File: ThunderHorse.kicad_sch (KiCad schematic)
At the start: 0 parts

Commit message: Schematic structure
Added new schematic sheets.
Updated the main project.
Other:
- added sheet ESC (ESC.kicad_sch)
- added sheet MCU (MCU.kicad_sch)
- added sheet Power (Power.kicad_sch)
- added sheet Sensors (Sensors.kicad_sch)
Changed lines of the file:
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@@
 		(company "Chapuzas S.L.")
+	)
+	(sheet
+		(at 52.07 92.71)
+		(size 88.9 58.42)
+		(exclude_from_sim no)
+		(in_bom yes)
+		(on_board yes)
+		(dnp no)
+		(fields_autoplaced yes)
+		(stroke
+			(width 0.1524)
+			(type solid)
+		)
+		(fill
+			(color 0 0 0 0.0000)
+		)
+		(property "Sheetname" "MCU"
+			(at 52.07 91.9984 0)
+			(effects
+				(font
+					(size 1.27 1.27)
+				)
+				(justify left bottom)
+			)
+		)
+		(property "Sheetfile" "MCU.kicad_sch"
+			(at 52.07 151.7146 0)
+			(effects
+				(font
+					(size 1.27 1.27)
+				)
+				(justify left top)
+			)
+		)
+		(instances
+			(project "ThunderHorse"
+				(path "/ac187c6c-fa53-41cc-bce1-6f39a42a92e8"
+					(page "3")
+				)
+			)
+		)
+	)
+	(sheet
+		(at 154.94 92.71)
+		(size 88.9 58.42)
+		(exclude_from_sim no)
+		(in_bom yes)
+		(on_board yes)
+		(dnp no)
+		(fields_autoplaced yes)
+		(stroke
+			(width 0.1524)
+			(type solid)
+		)
+		(fill
+			(color 0 0 0 0.0000)
+		)
+		(property "Sheetname" "Sensors"
+			(at 154.94 91.9984 0)
+			(effects
+				(font
+					(size 1.27 1.27)
+				)
+				(justify left bottom)
+			)
+		)
+		(property "Sheetfile" "Sensors.kicad_sch"
+			(at 154.94 151.7146 0)
+			(effects
+				(font
+					(size 1.27 1.27)
+				)
+				(justify left top)
+			)
+		)
+		(instances
+			(project "ThunderHorse"
+				(path "/ac187c6c-fa53-41cc-bce1-6f39a42a92e8"
+					(page "5")
+				)
+			)
+		)
+	)
+	(sheet
+		(at 154.94 26.67)
+		(size 88.9 58.42)
+		(exclude_from_sim no)
+		(in_bom yes)
+		(on_board yes)
+		(dnp no)
+		(fields_autoplaced yes)
+		(stroke
+			(width 0.1524)
+			(type solid)
+		)
+		(fill
+			(color 0 0 0 0.0000)
+		)
+		(property "Sheetname" "ESC"
+			(at 154.94 25.9584 0)
+			(effects
+				(font
+					(size 1.27 1.27)
+				)
+				(justify left bottom)
+			)
+		)
+		(property "Sheetfile" "ESC.kicad_sch"
+			(at 154.94 85.6746 0)
+			(effects
+				(font
+					(size 1.27 1.27)
+				)
+				(justify left top)
+			)
+		)
+		(instances
+			(project "ThunderHorse"
+				(path "/ac187c6c-fa53-41cc-bce1-6f39a42a92e8"
+					(page "4")
+				)
+			)
+		)
+	)
+	(sheet
+		(at 52.07 26.67)
+		(size 88.9 58.42)
+		(exclude_from_sim no)
+		(in_bom yes)
+		(on_board yes)
+		(dnp no)
+		(fields_autoplaced yes)
+		(stroke
+			(width 0.1524)
+			(type solid)
+		)
+		(fill
+			(color 0 0 0 0.0000)
+		)
+		(property "Sheetname" "Power"
+			(at 52.07 25.9584 0)
+			(effects
+				(font
+					(size 1.27 1.27)
+				)
+				(justify left bottom)
+			)
+		)
+		(property "Sheetfile" "Power.kicad_sch"
+			(at 52.07 85.6746 0)
+			(effects
+				(font
+					(size 1.27 1.27)
+				)
+				(justify left top)
+			)
+		)
+		(instances
+			(project "ThunderHorse"
+				(path "/ac187c6c-fa53-41cc-bce1-6f39a42a92e8"
+					(page "2")
+				)
+			)
+		)
 	)
 	(sheet_instances

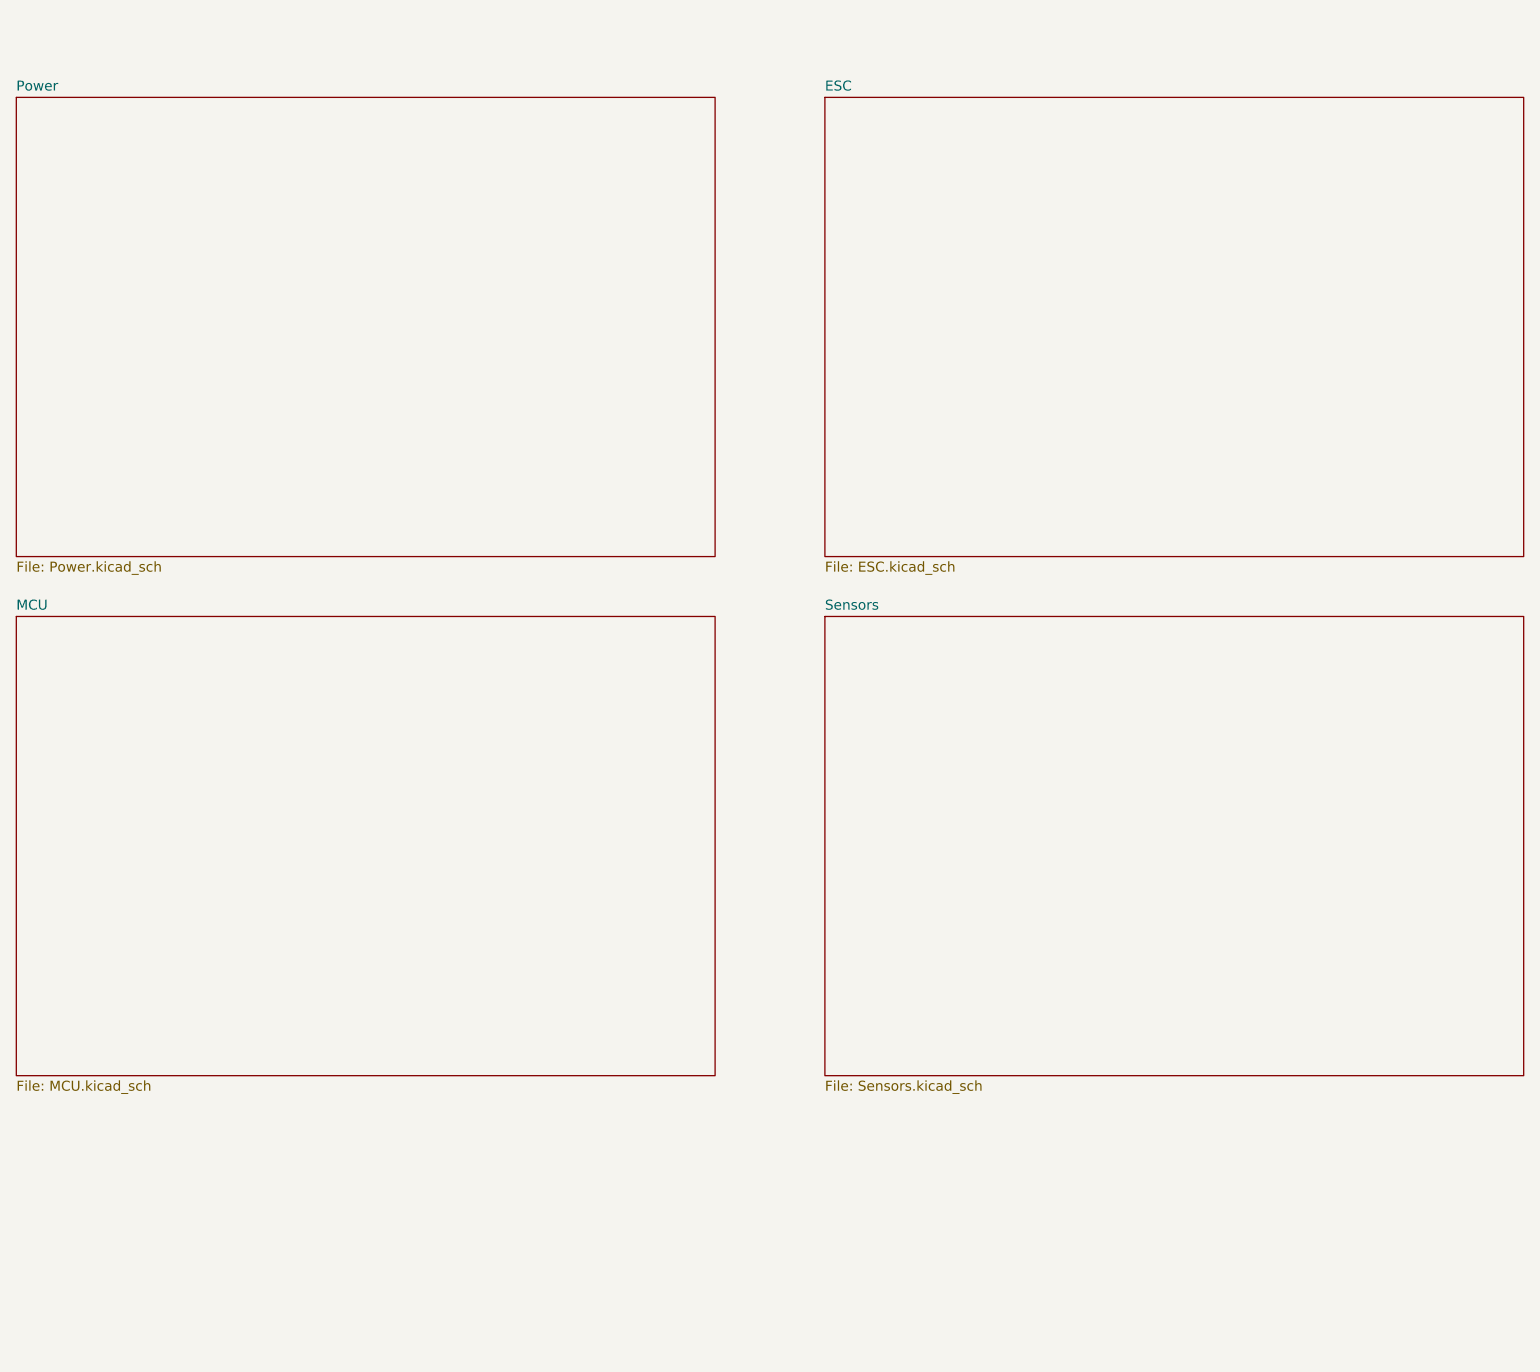
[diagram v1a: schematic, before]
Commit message: Receiver design
Updated the receiver design for the SX1280.
Added an ignore for lock files.
Minor schematic updates.
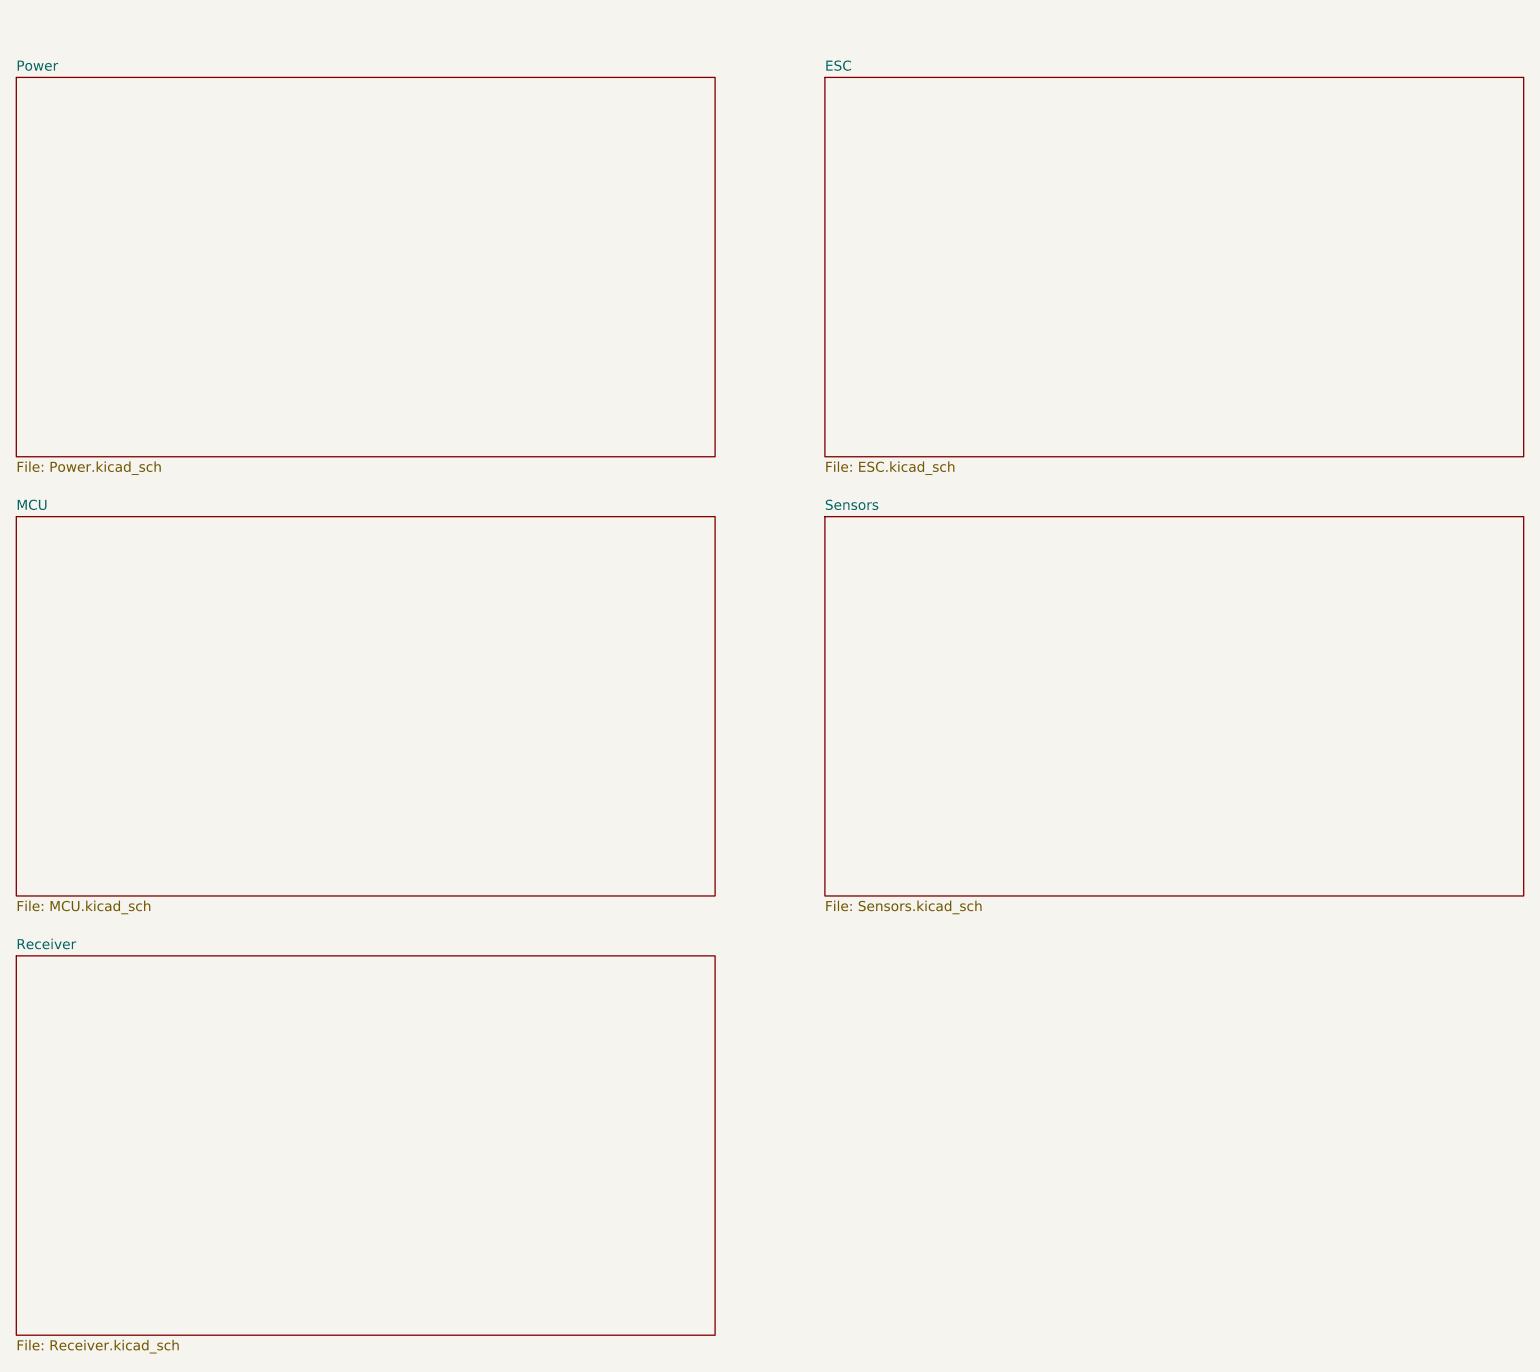
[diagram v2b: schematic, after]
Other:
- added sheet Receiver (Receiver.kicad_sch)
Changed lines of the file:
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@@
 	)
 	(sheet
-		(at 52.07 92.71)
-		(size 88.9 58.42)
+		(at 52.07 80.01)
+		(size 88.9 48.26)
 		(exclude_from_sim no)
 		(in_bom yes)
@@
 		)
 		(property "Sheetname" "MCU"
-			(at 52.07 91.9984 0)
+			(at 52.07 79.2984 0)
 			(effects
 				(font
@@
 		)
 		(property "Sheetfile" "MCU.kicad_sch"
-			(at 52.07 151.7146 0)
+			(at 52.07 128.8546 0)
 			(effects
 				(font
@@
 	)
 	(sheet
-		(at 154.94 92.71)
-		(size 88.9 58.42)
+		(at 154.94 80.01)
+		(size 88.9 48.26)
 		(exclude_from_sim no)
 		(in_bom yes)
@@
 		)
 		(property "Sheetname" "Sensors"
-			(at 154.94 91.9984 0)
+			(at 154.94 79.2984 0)
 			(effects
 				(font
@@
 		)
 		(property "Sheetfile" "Sensors.kicad_sch"
-			(at 154.94 151.7146 0)
+			(at 154.94 128.8546 0)
 			(effects
 				(font
@@
 	)
 	(sheet
-		(at 154.94 26.67)
-		(size 88.9 58.42)
+		(at 154.94 24.13)
+		(size 88.9 48.26)
 		(exclude_from_sim no)
 		(in_bom yes)
@@
 		)
 		(property "Sheetname" "ESC"
-			(at 154.94 25.9584 0)
+			(at 154.94 23.4184 0)
 			(effects
 				(font
@@
 		)
 		(property "Sheetfile" "ESC.kicad_sch"
-			(at 154.94 85.6746 0)
+			(at 154.94 72.9746 0)
 			(effects
 				(font
@@
 	)
 	(sheet
-		(at 52.07 26.67)
-		(size 88.9 58.42)
+		(at 52.07 24.13)
+		(size 88.9 48.26)
 		(exclude_from_sim no)
 		(in_bom yes)
@@
 		)
 		(property "Sheetname" "Power"
-			(at 52.07 25.9584 0)
+			(at 52.07 23.4184 0)
 			(effects
 				(font
@@
 		)
 		(property "Sheetfile" "Power.kicad_sch"
-			(at 52.07 85.6746 0)
+			(at 52.07 72.9746 0)
 			(effects
 				(font
@@
 				)
 			)
+		)
+	)
+	(sheet
+		(at 52.07 135.89)
+		(size 88.9 48.26)
+		(exclude_from_sim no)
+		(in_bom yes)
+		(on_board yes)
+		(dnp no)
+		(fields_autoplaced yes)
+		(stroke
+			(width 0.1524)
+			(type solid)
+		)
+		(fill
+			(color 0 0 0 0.0000)
+		)
+		(property "Sheetname" "Receiver"
+			(at 52.07 135.1784 0)
+			(effects
+				(font
+					(size 1.27 1.27)
+				)
+				(justify left bottom)
+			)
+		)
+		(property "Sheetfile" "Receiver.kicad_sch"
+			(at 52.07 184.7346 0)
+			(effects
+				(font
+					(size 1.27 1.27)
+				)
+				(justify left top)
+			)
+		)
+		(instances
+			(project "ThunderHorse"
+				(path "/ac187c6c-fa53-41cc-bce1-6f39a42a92e8"
+					(page "6")
+				)
+			)

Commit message: Power and MCU
Updated the power schematic.
Updated the MCU schematic.

TODO:
Merge with features branch.
Review all schematics prior to layout.
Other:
- added sheet Others (Others.kicad_sch)
- company: Chapuzas S.L. -> DavidMolTor
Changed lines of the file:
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@@
 		(date "2026-01-28")
 		(rev "1.0")
-		(company "Chapuzas S.L.")
-	)
-	(sheet
-		(at 52.07 80.01)
-		(size 88.9 48.26)
+		(company "DavidMolTor")
+	)
+	(sheet
+		(at 152.4 118.11)
+		(size 88.9 41.91)
+		(exclude_from_sim no)
+		(in_bom yes)
+		(on_board yes)
+		(dnp no)
+		(fields_autoplaced yes)
+		(stroke
+			(width 0.1524)
+			(type solid)
+		)
+		(fill
+			(color 0 0 0 0.0000)
+		)
+		(property "Sheetname" "Others"
+			(at 152.4 117.3984 0)
+			(effects
+				(font
+					(size 1.27 1.27)
+				)
+				(justify left bottom)
+			)
+		)
+		(property "Sheetfile" "Others.kicad_sch"
+			(at 152.4 160.6046 0)
+			(effects
+				(font
+					(size 1.27 1.27)
+				)
+				(justify left top)
+			)
+		)
+		(instances
+			(project "ThunderHorse"
+				(path "/ac187c6c-fa53-41cc-bce1-6f39a42a92e8"
+					(page "11")
+				)
+			)
+		)
+	)
+	(sheet
+		(at 54.61 68.58)
+		(size 88.9 41.91)
 		(exclude_from_sim no)
 		(in_bom yes)
@@
 		)
 		(property "Sheetname" "MCU"
-			(at 52.07 79.2984 0)
+			(at 54.61 67.8684 0)
 			(effects
 				(font
@@
 		)
 		(property "Sheetfile" "MCU.kicad_sch"
-			(at 52.07 128.8546 0)
+			(at 54.61 111.0746 0)
 			(effects
 				(font
@@
 	)
 	(sheet
-		(at 154.94 80.01)
-		(size 88.9 48.26)
+		(at 152.4 68.58)
+		(size 88.9 41.91)
 		(exclude_from_sim no)
 		(in_bom yes)
@@
 		)
 		(property "Sheetname" "Sensors"
-			(at 154.94 79.2984 0)
+			(at 152.4 67.8684 0)
 			(effects
 				(font
@@
 		)
 		(property "Sheetfile" "Sensors.kicad_sch"
-			(at 154.94 128.8546 0)
-			(effects
-				(font
-					(size 1.27 1.27)
-				)
-				(justify left top)
-			)
-		)
-		(instances
-			(project "ThunderHorse"
-				(path "/ac187c6c-fa53-41cc-bce1-6f39a42a92e8"
-					(page "5")
-				)
-			)
-		)
-	)
-	(sheet
-		(at 154.94 24.13)
-		(size 88.9 48.26)
+			(at 152.4 111.0746 0)
+			(effects
+				(font
+					(size 1.27 1.27)
+				)
+				(justify left top)
+			)
+		)
+		(instances
+			(project "ThunderHorse"
+				(path "/ac187c6c-fa53-41cc-bce1-6f39a42a92e8"
+					(page "9")
+				)
+			)
+		)
+	)
+	(sheet
+		(at 152.4 19.05)
+		(size 88.9 41.91)
 		(exclude_from_sim no)
 		(in_bom yes)
@@
 		)
 		(property "Sheetname" "ESC"
-			(at 154.94 23.4184 0)
+			(at 152.4 18.3384 0)
 			(effects
 				(font
@@
 		)
 		(property "Sheetfile" "ESC.kicad_sch"
-			(at 154.94 72.9746 0)
+			(at 152.4 61.5446 0)
 			(effects
 				(font
@@
 	)
 	(sheet
-		(at 52.07 24.13)
-		(size 88.9 48.26)
+		(at 54.61 19.05)
+		(size 88.9 41.91)
 		(exclude_from_sim no)
 		(in_bom yes)
@@
 		)
 		(property "Sheetname" "Power"
-			(at 52.07 23.4184 0)
+			(at 54.61 18.3384 0)
 			(effects
 				(font
@@
 		)
 		(property "Sheetfile" "Power.kicad_sch"
-			(at 52.07 72.9746 0)
+			(at 54.61 61.5446 0)
 			(effects
 				(font
@@
 	)
 	(sheet
-		(at 52.07 135.89)
-		(size 88.9 48.26)
+		(at 54.61 118.11)
+		(size 88.9 41.91)
 		(exclude_from_sim no)
 		(in_bom yes)
@@
 		)
 		(property "Sheetname" "Receiver"
-			(at 52.07 135.1784 0)
+			(at 54.61 117.3984 0)
 			(effects
 				(font
@@
 		)
 		(property "Sheetfile" "Receiver.kicad_sch"
-			(at 52.07 184.7346 0)
-			(effects
-				(font
-					(size 1.27 1.27)
-				)
-				(justify left top)
-			)
-		)
-		(instances
-			(project "ThunderHorse"
-				(path "/ac187c6c-fa53-41cc-bce1-6f39a42a92e8"
-					(page "6")
-				)
-			)
+			(at 54.61 160.6046 0)
+			(effects
+				(font
+					(size 1.27 1.27)
+				)
+				(justify left top)
+			)
+		)
+		(instances
+			(project "ThunderHorse"
+				(path "/ac187c6c-fa53-41cc-bce1-6f39a42a92e8"
+					(page "10")
+				)
+			)
